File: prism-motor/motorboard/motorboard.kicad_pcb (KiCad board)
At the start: 4 copper layers, 20.1 x 25.4 mm, 5 parts, among them J1 Conn_01x03, J2 Conn_01x03, U1 DRV5015A3QDBZR

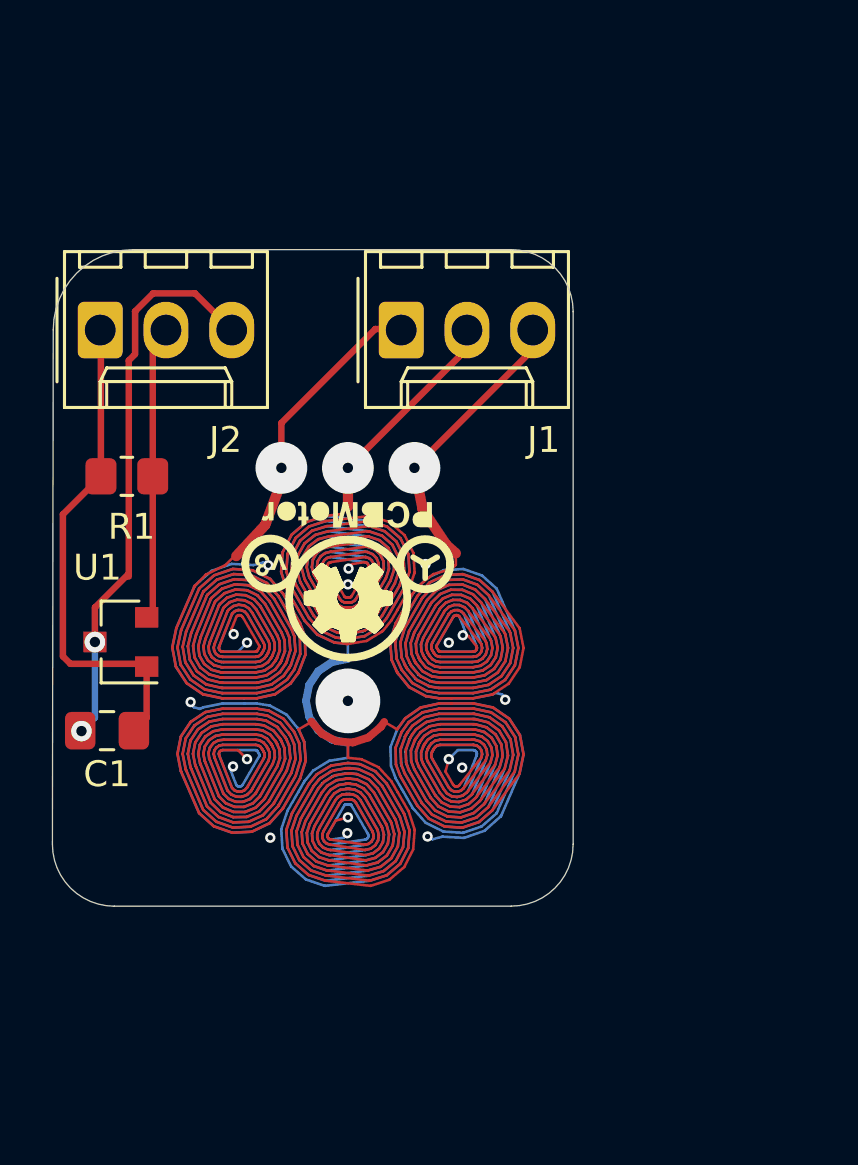
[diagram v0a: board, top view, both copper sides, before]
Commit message: adapted motor and ESP32 shield
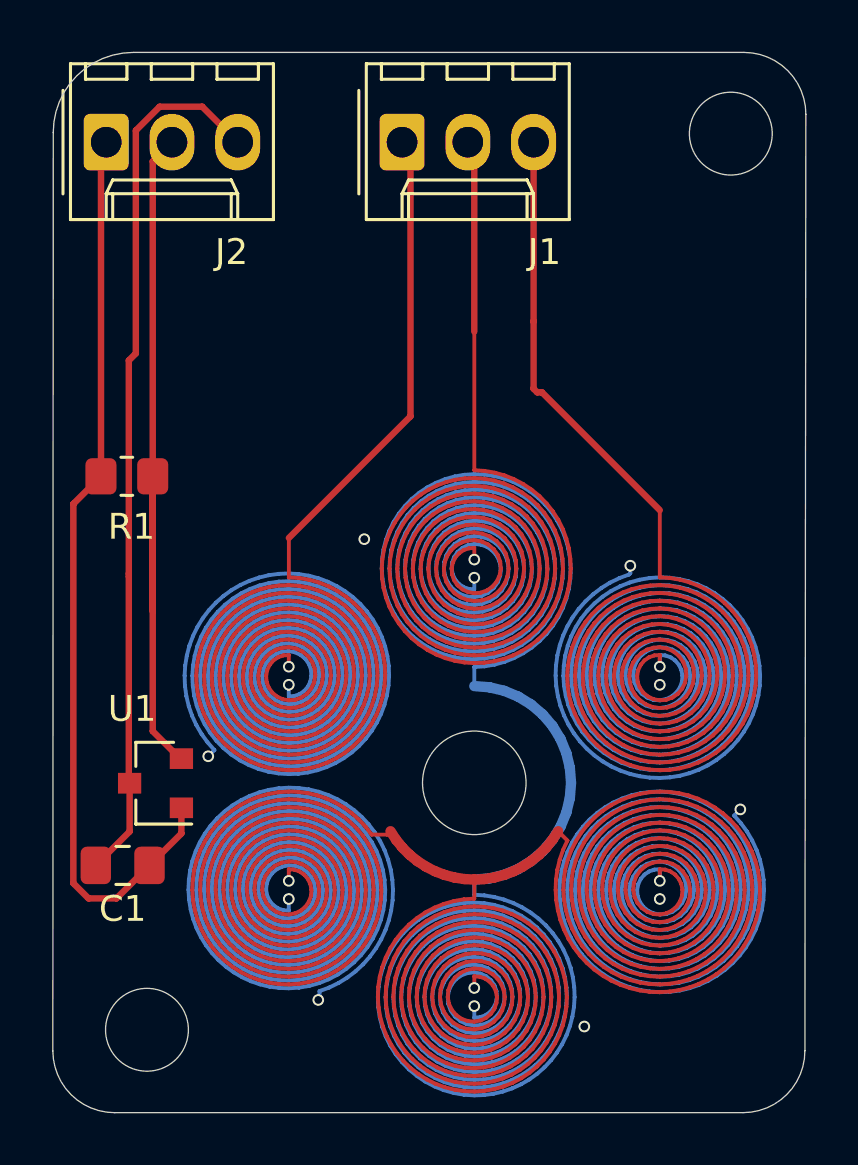
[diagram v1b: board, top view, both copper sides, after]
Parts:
- moved J2 7.26 mm to (116.2, 82.5)
- moved J1 7.26 mm to (127.6, 82.5)
- moved U1 5.62 mm to (118.1, 107.3)
- moved C1 5.24 mm to (116.8, 110.5)
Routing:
- net PH1: track 2468.4 -> 3885.7 mm, vias 21 -> 18
- net HALL: track 12.2 -> 29.8 mm
- net +3V3: track 19.3 -> 36.0 mm
- net GND: track 21.8 -> 33.7 mm, vias 2 -> 0
- net (no net): track 6.56 -> 0.00 mm, vias 1 -> 0
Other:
- board size 20.1 x 25.4 mm -> 29.1 x 41 mm
- net class Default: clearance 0.2 -> 0.15; trace_width 0.25 -> 0.15; via_dia 0.8 -> 0.45; via_drill 0.4 -> 0.3
- rule trace_clearance: 0.2 -> 0.15
- rule trace_min: 0.1 -> 0.15
- board text removed: "error of center hole too close to via is ignored"

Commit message: started with compact for version of laserhead
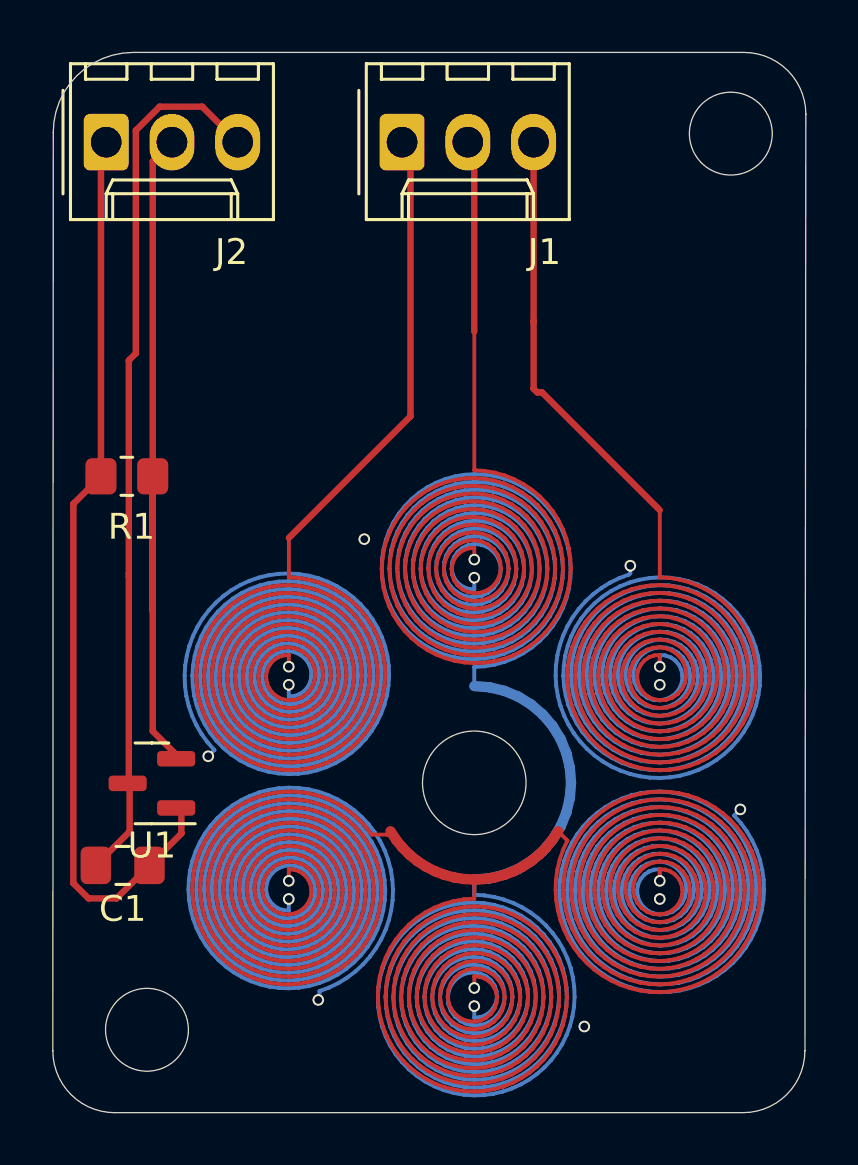
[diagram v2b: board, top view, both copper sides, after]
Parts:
- moved U1 0.14 mm to (118.0, 107.3)
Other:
- net class Default removed
